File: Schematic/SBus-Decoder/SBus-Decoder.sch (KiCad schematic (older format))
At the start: 10 parts, among them J1 Conn_01x03_Male, J2 Conn_01x01_Male, J3 Conn_02x03_Odd_Even, U1 PIC16F18313-I_SN, U2 MCP1703A-3302_SOT23

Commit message: Schematic and pcb
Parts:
- removed J3: Conn_02x03_Odd_Even, Connector_PinHeader_2.54mm:PinHeader_2x03_P2.54mm_Horizontal, symbol Connector_Generic:Conn_02x03_Odd_Even
- removed U1: PIC16F18313-I_SN, PIC16F18313:PIC16F18313-I&slash_SN, symbol PIC16F18313:PIC16F18313-I_SN
- added J3: Conn_01x01_Male, Connector_PinHeader_2.54mm:PinHeader_1x01_P2.54mm_Vertical, symbol Connector:Conn_01x01_Male
- added J4: TSW-104-08-G-T-RA, HDRRA12W64P254_3X4_1016X254X810P, symbol SamacSys_Parts:TSW-104-08-G-T-RA
- added U1: PIC18F04Q40-I_ST, PIC18F0xQ40:PIC18F04Q40-I&slash_ST, symbol PIC18F0xQ40:PIC18F04Q40-I_ST
- J1: footprint Connector_Wire:SolderWire-0.75sqmm_1x03_P4.8mm_D1.25mm_OD2.3mm -> Connector_Wire:SolderWire-0.5sqmm_1x03_P4.6mm_D0.9mm_OD2.1mm
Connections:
- net +3V3: now also U1.1 (VDD)
- net GND: now also J4.12, J4.3, J4.6, J4.9, U1.14 (VSS)
- net VBUS: now also J4.11, J4.2, J4.5, J4.8
- net at J1.1 (Pin_1): now also U1.7 (RC3)
- net at R1.2: now also U1.8 (RC2)
- new net: J4.7, U1.10 (RC0)
- new net: J4.4, U1.12 (RA1/ICSPCLK)
- new net: J4.1, U1.13 (RA0/ICSPDAT)
- new net: J3.1 (Pin_1), U1.4 (*MCLR/VPP/RA3)
- new net: J4.10, U1.9 (RC1)
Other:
- note added: "ICSP\nMLCR"
- note added: "SBUS In"
- note added: "Servos 1-4"
- note removed: "SBUS In/Out"
- note removed: "Servo 1"
- note removed: "Servo 2"
- moved on the sheet: J1, J2
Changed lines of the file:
@@
 $EndDescr
-$Comp
-L PIC16F18313:PIC16F18313-I_SN U1
-U 1 1 60EFBC4A
-P 4000 3650
-F 0 "U1" H 5400 4037 60  0000 C CNN
-F 1 "PIC16F18313-I_SN" H 5400 3931 60  0000 C CNN
-F 2 "PIC16F18313:PIC16F18313-I&slash_SN" H 5400 3890 60  0001 C CNN
-F 3 "" H 4000 3650 60  0000 C CNN
-	1    4000 3650
-	1    0    0    -1
-$EndComp
 $Comp
 L Device:C C1
@@
 	1    0    0    -1
 $EndComp
-$Comp
-L Connector:Conn_01x03_Male J1
-U 1 1 60F0F0EB
-P 1300 1700
-F 0 "J1" V 1300 1900 50  0000 C CNN
-F 1 "Conn_01x03_Male" H 1408 1890 50  0001 C CNN
-F 2 "Connector_Wire:SolderWire-0.75sqmm_1x03_P4.8mm_D1.25mm_OD2.3mm" H 1300 1700 50  0001 C CNN
-F 3 "~" H 1300 1700 50  0001 C CNN
-	1    1300 1700
-	0    -1   1    0
-$EndComp
-Text Notes 1450 1550 0    50   ~ 0
-SBUS In/Out
-Text Notes 7200 3900 0    50   ~ 0
-Servo 1
-Text Notes 8550 3900 0    50   ~ 0
-Servo 2
-Text Notes 3350 4900 0    50   ~ 0
+Text Notes 1800 4250 0    50   ~ 0
+SBUS In
+Text Notes 2850 3150 0    50   ~ 0
 ICSP \nVdd
 Wire Wire Line
-	4000 3650 3450 3650
-Wire Wire Line
-	3450 3650 3450 4450
-Wire Wire Line
 	5550 2950 6150 2950
 Wire Wire Line
 	6800 2950 6800 3650
-Wire Wire Line
-	3450 2950 3450 3650
-Connection ~ 3450 3650
 Wire Wire Line
 	6150 3050 6150 2950
@@
 Wire Wire Line
 	5950 1750 5200 1750
-Wire Wire Line
-	6800 3850 7100 3850
 $Comp
 L power:VBUS #PWR09
@@
 L power:VBUS #PWR01
 U 1 1 60F33FE8
-P 900 2100
-F 0 "#PWR01" H 900 1950 50  0001 C CNN
-F 1 "VBUS" V 915 2227 50  0000 L CNN
-F 2 "" H 900 2100 50  0001 C CNN
-F 3 "" H 900 2100 50  0001 C CNN
-	1    900  2100
-	0    -1   -1   0
-$EndComp
-Wire Wire Line
-	900  2100 1300 2100
-Wire Wire Line
-	1300 2100 1300 1900
-Wire Wire Line
-	1200 1900 1200 2300
-Wire Wire Line
-	1200 2300 1950 2300
+P 2450 4600
+F 0 "#PWR01" H 2450 4450 50  0001 C CNN
+F 1 "VBUS" V 2465 4727 50  0000 L CNN
+F 2 "" H 2450 4600 50  0001 C CNN
+F 3 "" H 2450 4600 50  0001 C CNN
+	1    2450 4600
+	0    1    1    0
+$EndComp
 $Comp
 L power:GND #PWR08
@@
 $EndComp
 Wire Wire Line
-	6800 3950 6900 3950
-Wire Wire Line
-	6900 3950 6900 4500
-Wire Wire Line
 	6900 4800 6900 5150
 Wire Wire Line
@@
 Wire Wire Line
 	3450 2950 3450 2750
-Connection ~ 3450 2950
 Wire Wire Line
 	6250 1000 6250 1250
-Wire Wire Line
-	1950 2300 1950 3950
-Wire Wire Line
-	4000 3850 3900 3850
-Wire Wire Line
-	3900 3850 3900 3750
-Wire Wire Line
-	3900 3750 4000 3750
-Wire Wire Line
-	1950 3950 4000 3950
 $Comp
 L Connector:Conn_01x01_Male J2
 U 1 1 60F2444D
-P 3450 4650
-F 0 "J2" V 3558 4562 50  0000 R CNN
-F 1 "Conn_01x01_Male" V 3513 4562 50  0001 R CNN
-F 2 "Connector_PinHeader_2.54mm:PinHeader_1x01_P2.54mm_Vertical" H 3450 4650 50  0001 C CNN
-F 3 "~" H 3450 4650 50  0001 C CNN
-	1    3450 4650
-	0    -1   -1   0
+P 2950 3200
+F 0 "J2" V 3058 3112 50  0000 R CNN
+F 1 "Conn_01x01_Male" V 3013 3112 50  0001 R CNN
+F 2 "Connector_PinHeader_2.54mm:PinHeader_1x01_P2.54mm_Vertical" H 2950 3200 50  0001 C CNN
+F 3 "~" H 2950 3200 50  0001 C CNN
+	1    2950 3200
+	0    1    1    0
 $EndComp
 $Comp
@@
 L power:GND #PWR02
 U 1 1 60F5D84A
-P 1650 2100
-F 0 "#PWR02" H 1650 1850 50  0001 C CNN
-F 1 "GND" H 1650 1950 50  0000 C CNN
-F 2 "" H 1650 2100 50  0001 C CNN
-F 3 "" H 1650 2100 50  0001 C CNN
-	1    1650 2100
-	1    0    0    -1
-$EndComp
-Wire Wire Line
-	1400 2100 1650 2100
-Wire Wire Line
-	1400 1900 1400 2100
-Wire Wire Line
-	8150 3950 8250 3950
-Wire Wire Line
-	8250 3950 8250 4150
-Wire Wire Line
-	8250 4150 7900 4150
-Wire Wire Line
-	7900 4150 7900 4200
-Wire Wire Line
-	7650 3950 7500 3950
-Wire Wire Line
-	7500 3950 7500 4150
-Connection ~ 7900 4150
-Wire Wire Line
-	7100 4450 8450 4450
-Wire Wire Line
-	8450 3750 8150 3750
-Wire Wire Line
-	7500 4150 7900 4150
-Wire Wire Line
-	8450 3750 8450 4450
-Wire Wire Line
-	8150 3850 8250 3850
-Wire Wire Line
-	8250 3850 8250 3300
-Wire Wire Line
-	8250 3300 7850 3300
-Wire Wire Line
-	7650 3850 7550 3850
-Wire Wire Line
-	7550 3850 7550 3300
-Wire Wire Line
-	7550 3300 7850 3300
+P 2450 4700
+F 0 "#PWR02" H 2450 4450 50  0001 C CNN
+F 1 "GND" H 2450 4550 50  0000 C CNN
+F 2 "" H 2450 4700 50  0001 C CNN
+F 3 "" H 2450 4700 50  0001 C CNN
+	1    2450 4700
+	1    0    0    -1
+$EndComp
+$Comp
+L PIC18F0xQ40:PIC18F04Q40-I_ST U1
+U 1 1 60F62A13
+P 3550 3650
+F 0 "U1" H 5050 4037 60  0000 C CNN
+F 1 "PIC18F04Q40-I_ST" H 5050 3931 60  0000 C CNN
+F 2 "PIC18F0xQ40:PIC18F04Q40-I&slash_ST" H 5050 3890 60  0001 C CNN
+F 3 "" H 3550 3650 60  0000 C CNN
+	1    3550 3650
+	1    0    0    -1
+$EndComp
+$Comp
+L Connector:Conn_01x01_Male J3
+U 1 1 60F6C0D6
+P 2650 3200
+F 0 "J3" V 2758 3112 50  0000 R CNN
+F 1 "Conn_01x01_Male" V 2713 3112 50  0001 R CNN
+F 2 "Connector_PinHeader_2.54mm:PinHeader_1x01_P2.54mm_Vertical" H 2650 3200 50  0001 C CNN
+F 3 "~" H 2650 3200 50  0001 C CNN
+	1    2650 3200
+	0    1    1    0
+$EndComp
+Text Notes 2550 3150 0    50   ~ 0
+ICSP\nMLCR
+$Comp
+L Connector:Conn_01x03_Male J1
+U 1 1 60F0F0EB
+P 1950 4600
+F 0 "J1" V 1950 4800 50  0000 C CNN
+F 1 "Conn_01x03_Male" H 2058 4790 50  0001 C CNN
+F 2 "Connector_Wire:SolderWire-0.5sqmm_1x03_P4.6mm_D0.9mm_OD2.1mm" H 1950 4600 50  0001 C CNN
+F 3 "~" H 1950 4600 50  0001 C CNN
+	1    1950 4600
+	1    0    0    -1
+$EndComp
+$Comp
+L SamacSys_Parts:TSW-104-08-G-T-RA J4
+U 1 1 60F70215
+P 8100 3550
+F 0 "J4" H 8550 3723 50  0000 C CNN
+F 1 "TSW-104-08-G-T-RA" H 8550 3724 50  0001 C CNN
+F 2 "HDRRA12W64P254_3X4_1016X254X810P" H 8850 3650 50  0001 L CNN
+F 3 "http://suddendocs.samtec.com/catalog_english/tsw_th.pdf" H 8850 3550 50  0001 L CNN
+F 4 "CONN HEADER 12 POS .100\"" H 8850 3450 50  0001 L CNN "Description"
+F 5 "8.1" H 8850 3350 50  0001 L CNN "Height"
+F 6 "200-TSW10408GTRA" H 8850 3250 50  0001 L CNN "Mouser Part Number"
+F 7 "https://www.mouser.co.uk/ProductDetail/Samtec/TSW-104-08-G-T-RA?qs=rU5fayqh%252BE1gavtOYeKUlQ%3D%3D" H 8850 3150 50  0001 L CNN "Mouser Price/Stock"
+F 8 "SAMTEC" H 8850 3050 50  0001 L CNN "Manufacturer_Name"
+F 9 "TSW-104-08-G-T-RA" H 8850 2950 50  0001 L CNN "Manufacturer_Part_Number"
+	1    8100 3550
+	1    0    0    -1
+$EndComp
+Wire Wire Line
+	2150 4700 2450 4700
+Wire Wire Line
+	2150 4600 2450 4600
+Wire Wire Line
+	3550 3650 3450 3650
+Wire Wire Line
+	3450 3650 3450 3400
+Connection ~ 3450 2950
+Wire Wire Line
+	2950 3400 3450 3400
+Connection ~ 3450 3400
+Wire Wire Line
+	3450 3400 3450 2950
+Wire Wire Line
+	6550 3650 6800 3650
+Wire Wire Line
+	6550 4250 6900 4250
+Wire Wire Line
+	6900 4250 6900 4500
+Wire Wire Line
+	6550 3750 7300 3750
+Wire Wire Line
+	7300 3750 7300 3550
+Wire Wire Line
+	7300 3550 8100 3550
+Wire Wire Line
+	6550 3850 7600 3850
+Wire Wire Line
+	7600 3850 7600 2900
+Wire Wire Line
+	7600 2900 9300 2900
+Wire Wire Line
+	9300 2900 9300 3650
+Wire Wire Line
+	9300 3650 9000 3650
+Wire Wire Line
+	6550 4050 7800 4050
+Wire Wire Line
+	7800 4050 7800 3850
+Wire Wire Line
+	7800 3850 8100 3850
+Wire Wire Line
+	6550 4150 7500 4150
+Wire Wire Line
+	7500 4150 7500 4550
+Wire Wire Line
+	7500 4550 9350 4550
+Wire Wire Line
+	9350 4550 9350 3950
+Wire Wire Line
+	9350 3950 9000 3950
+Wire Wire Line
+	8100 3650 7900 3650
+Wire Wire Line
+	7900 3650 7900 3950
+Wire Wire Line
+	8100 3950 7900 3950
+Connection ~ 7900 3950
+Wire Wire Line
+	7900 3950 7900 4200
+$Comp
+L power:GND #PWR011
+U 1 1 60F7DF73
+P 9150 4200
+F 0 "#PWR011" H 9150 3950 50  0001 C CNN
+F 1 "GND" H 9155 4027 50  0000 C CNN
+F 2 "" H 9150 4200 50  0001 C CNN
+F 3 "" H 9150 4200 50  0001 C CNN
+	1    9150 4200
+	1    0    0    -1
+$EndComp
+Wire Wire Line
+	9000 3750 9150 3750
+Wire Wire Line
+	9150 3750 9150 4050
+Wire Wire Line
+	9000 4050 9150 4050
+Connection ~ 9150 4050
+Wire Wire Line
+	9150 4050 9150 4200
+Wire Wire Line
+	8100 3750 7850 3750
+Wire Wire Line
+	7850 3750 7850 3300
+Wire Wire Line
+	8100 4050 7850 4050
+Wire Wire Line
+	7850 4050 7850 3750
+Connection ~ 7850 3750
+Wire Wire Line
+	9000 3550 9050 3550
+Wire Wire Line
+	9050 3550 9050 3300
+Wire Wire Line
+	9050 3300 7850 3300
 Connection ~ 7850 3300
 Wire Wire Line
-	7100 3850 7100 4450
-Wire Wire Line
-	6800 3750 7650 3750
-$Comp
-L Connector_Generic:Conn_02x03_Odd_Even J3
-U 1 1 60F76AF8
-P 7850 3850
-F 0 "J3" H 7900 4075 50  0000 C CNN
-F 1 "Conn_02x03_Odd_Even" H 7900 4076 50  0001 C CNN
-F 2 "Connector_PinHeader_2.54mm:PinHeader_2x03_P2.54mm_Horizontal" H 7850 3850 50  0001 C CNN
-F 3 "~" H 7850 3850 50  0001 C CNN
-	1    7850 3850
-	1    0    0    -1
-$EndComp
+	9000 3850 9050 3850
+Wire Wire Line
+	9050 3850 9050 3550
+Connection ~ 9050 3550
+Text Notes 8350 4350 0    50   ~ 0
+Servos 1-4
+Wire Wire Line
+	2650 3400 2650 3950
+Wire Wire Line
+	2650 3950 3550 3950
+Wire Wire Line
+	2150 4500 2900 4500
+Wire Wire Line
+	2900 4500 2900 4250
+Wire Wire Line
+	2900 4250 3550 4250
 $EndSCHEMATC

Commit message: Changed input connector footprint
Using a 2.54 pin header will allow for more flexibility for other uses (like a servo sequencer.)
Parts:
- J1: footprint Connector_Wire:SolderWire-0.5sqmm_1x03_P4.6mm_D0.9mm_OD2.1mm -> Connector_PinHeader_2.54mm:PinHeader_1x03_P2.54mm_Vertical
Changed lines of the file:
@@
 F 0 "J1" V 1950 4800 50  0000 C CNN
 F 1 "Conn_01x03_Male" H 2058 4790 50  0001 C CNN
-F 2 "Connector_Wire:SolderWire-0.5sqmm_1x03_P4.6mm_D0.9mm_OD2.1mm" H 1950 4600 50  0001 C CNN
+F 2 "Connector_PinHeader_2.54mm:PinHeader_1x03_P2.54mm_Vertical" H 1950 4600 50  0001 C CNN
 F 3 "~" H 1950 4600 50  0001 C CNN
 	1    1950 4600

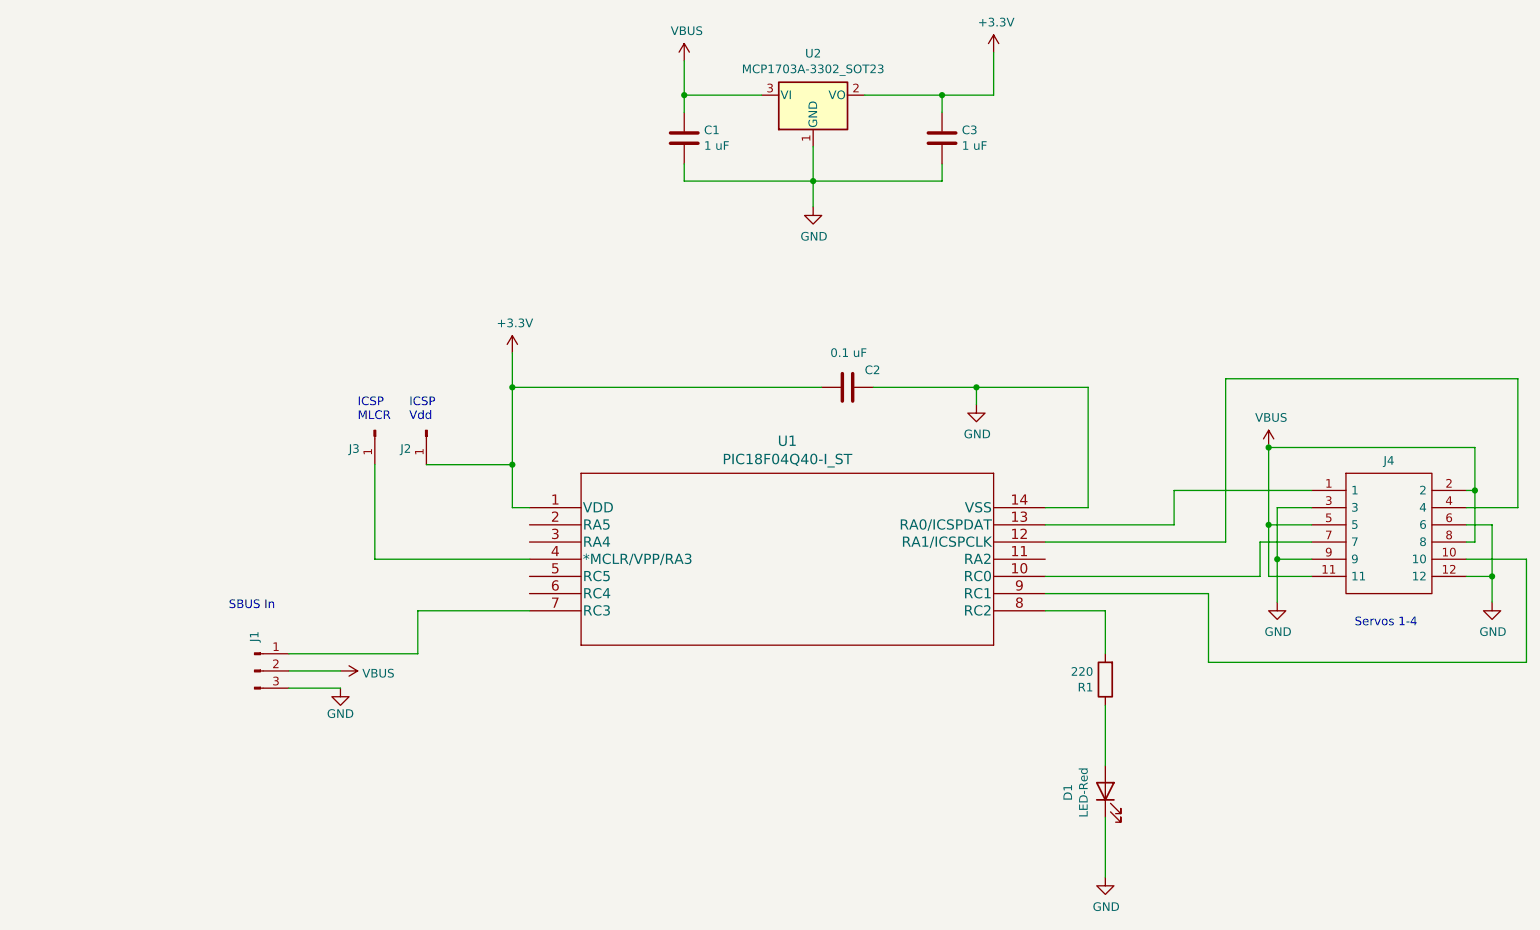
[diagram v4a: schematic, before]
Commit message: Better ICSP setup
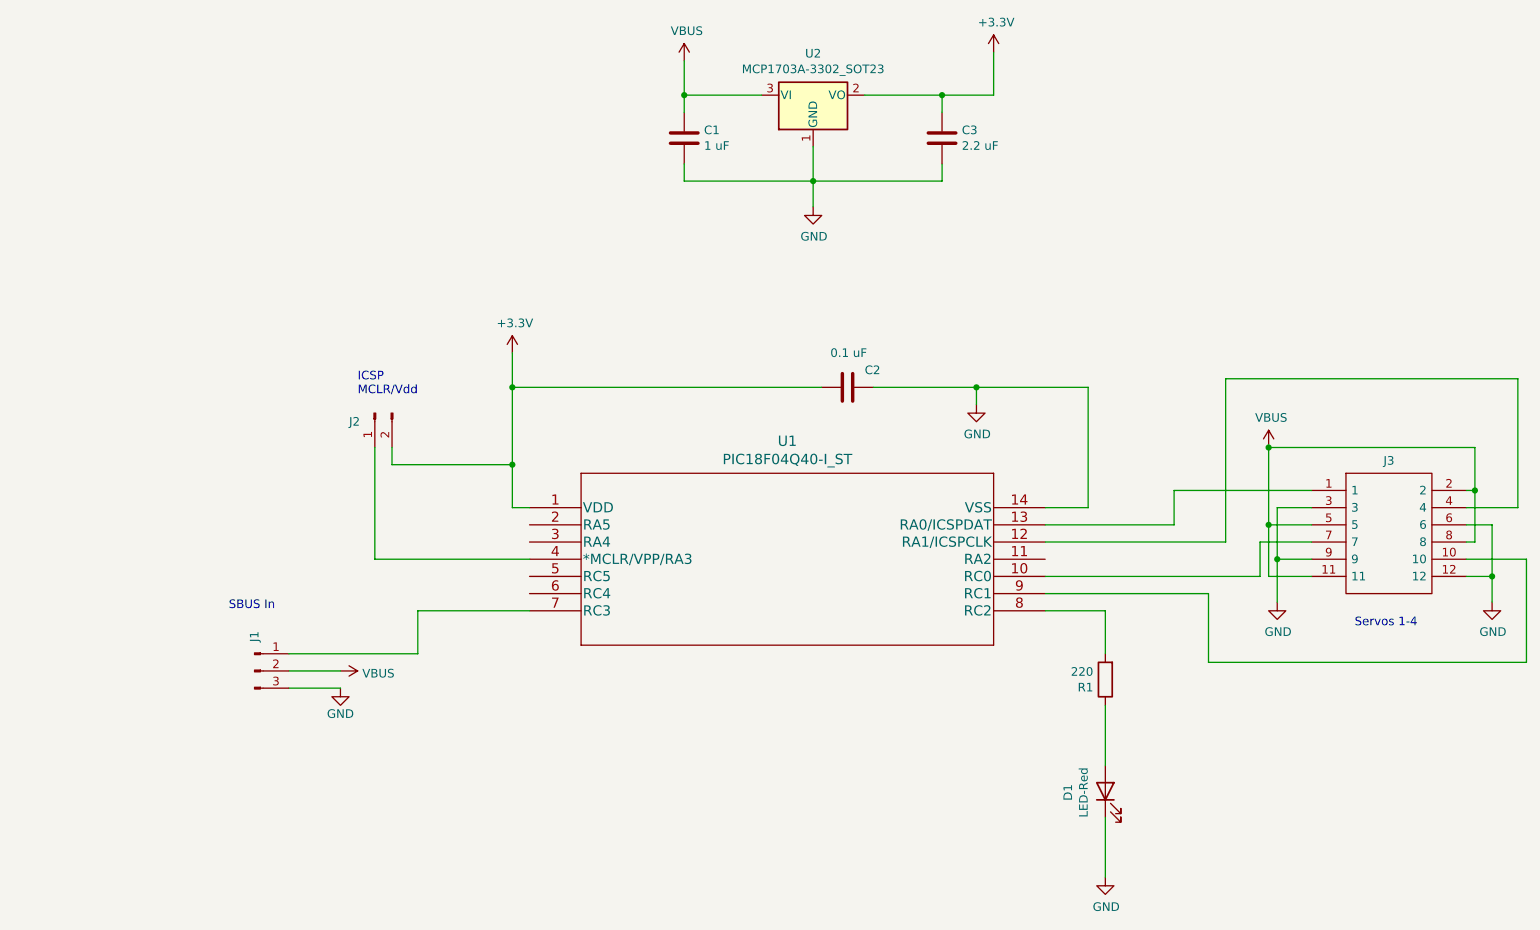
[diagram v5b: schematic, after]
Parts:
- removed J2, J3: Conn_01x01_Male, Connector_PinHeader_2.54mm:PinHeader_1x01_P2.54mm_Vertical, symbol Connector:Conn_01x01_Male
- added J2: Conn_01x02_Male, Connector_PinHeader_2.54mm:PinHeader_1x02_P2.54mm_Vertical, symbol Connector:Conn_01x02_Male
- C3: value 1 uF -> 2.2 uF
- renumbered J4 to J3
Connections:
- net +3V3: now also J2.2 (Pin_2)
- net at U1.4 (*MCLR/VPP/RA3): now also J2.1 (Pin_1)
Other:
- note added: "ICSP \nMCLR/Vdd"
- note removed: "ICSP \nVdd"
- note removed: "ICSP\nMLCR"
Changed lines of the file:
@@
 P 5950 1500
 F 0 "C3" H 6065 1546 50  0000 L CNN
-F 1 "1 uF" H 6065 1455 50  0000 L CNN
+F 1 "2.2 uF" H 6065 1455 50  0000 L CNN
 F 2 "Capacitor_SMD:C_0603_1608Metric" H 5988 1350 50  0001 C CNN
 F 3 "~" H 5950 1500 50  0001 C CNN
@@
 Text Notes 1800 4250 0    50   ~ 0
 SBUS In
-Text Notes 2850 3150 0    50   ~ 0
-ICSP \nVdd
+Text Notes 2550 3000 0    50   ~ 0
+ICSP \nMCLR/Vdd
 Wire Wire Line
 	5550 2950 6150 2950
@@
 	6250 1000 6250 1250
 $Comp
-L Connector:Conn_01x01_Male J2
-U 1 1 60F2444D
-P 2950 3200
-F 0 "J2" V 3058 3112 50  0000 R CNN
-F 1 "Conn_01x01_Male" V 3013 3112 50  0001 R CNN
-F 2 "Connector_PinHeader_2.54mm:PinHeader_1x01_P2.54mm_Vertical" H 2950 3200 50  0001 C CNN
-F 3 "~" H 2950 3200 50  0001 C CNN
-	1    2950 3200
-	0    1    1    0
-$EndComp
-$Comp
 L Regulator_Linear:MCP1703A-3302_SOT23 U2
 U 1 1 60F50A9F
@@
 $EndComp
 $Comp
-L Connector:Conn_01x01_Male J3
-U 1 1 60F6C0D6
-P 2650 3200
-F 0 "J3" V 2758 3112 50  0000 R CNN
-F 1 "Conn_01x01_Male" V 2713 3112 50  0001 R CNN
-F 2 "Connector_PinHeader_2.54mm:PinHeader_1x01_P2.54mm_Vertical" H 2650 3200 50  0001 C CNN
-F 3 "~" H 2650 3200 50  0001 C CNN
-	1    2650 3200
-	0    1    1    0
-$EndComp
-Text Notes 2550 3150 0    50   ~ 0
-ICSP\nMLCR
-$Comp
 L Connector:Conn_01x03_Male J1
 U 1 1 60F0F0EB
@@
 $EndComp
 $Comp
-L SamacSys_Parts:TSW-104-08-G-T-RA J4
+L SamacSys_Parts:TSW-104-08-G-T-RA J3
 U 1 1 60F70215
 P 8100 3550
-F 0 "J4" H 8550 3723 50  0000 C CNN
+F 0 "J3" H 8550 3723 50  0000 C CNN
 F 1 "TSW-104-08-G-T-RA" H 8550 3724 50  0001 C CNN
 F 2 "HDRRA12W64P254_3X4_1016X254X810P" H 8850 3650 50  0001 L CNN
@@
 	3450 3650 3450 3400
 Connection ~ 3450 2950
-Wire Wire Line
-	2950 3400 3450 3400
 Connection ~ 3450 3400
 Wire Wire Line
@@
 Servos 1-4
 Wire Wire Line
-	2650 3400 2650 3950
-Wire Wire Line
 	2650 3950 3550 3950
 Wire Wire Line
@@
 Wire Wire Line
 	2900 4250 3550 4250
+$Comp
+L Connector:Conn_01x02_Male J2
+U 1 1 60F7C777
+P 2650 3100
+F 0 "J2" V 2700 3250 50  0000 R CNN
+F 1 "Conn_01x02_Male" V 2803 2912 50  0001 R CNN
+F 2 "Connector_PinHeader_2.54mm:PinHeader_1x02_P2.54mm_Vertical" H 2650 3100 50  0001 C CNN
+F 3 "~" H 2650 3100 50  0001 C CNN
+	1    2650 3100
+	0    -1   1    0
+$EndComp
+Wire Wire Line
+	2650 3300 2650 3950
+Wire Wire Line
+	2750 3400 2750 3300
+Wire Wire Line
+	2750 3400 3450 3400
 $EndSCHEMATC
